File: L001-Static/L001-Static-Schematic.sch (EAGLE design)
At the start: 16 parts

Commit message: Fixes
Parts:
- R1, R2, R3, R4, R5, R6, R7, R8: value 10k -> 1K
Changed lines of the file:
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@@
 </classes>
 <parts>
-<part name="R1" library="resistor" deviceset="R-US_" device="VMTA55" value="10k"/>
-<part name="R2" library="resistor" deviceset="R-US_" device="VMTA55" value="10k"/>
-<part name="R3" library="resistor" deviceset="R-US_" device="VMTA55" value="10k"/>
-<part name="R4" library="resistor" deviceset="R-US_" device="VMTA55" value="10k"/>
-<part name="R5" library="resistor" deviceset="R-US_" device="VMTA55" value="10k"/>
-<part name="R6" library="resistor" deviceset="R-US_" device="VMTA55" value="10k"/>
-<part name="R7" library="resistor" deviceset="R-US_" device="VMTA55" value="10k"/>
-<part name="R8" library="resistor" deviceset="R-US_" device="VMTA55" value="10k"/>
+<part name="R1" library="resistor" deviceset="R-US_" device="VMTA55" value="1K"/>
+<part name="R2" library="resistor" deviceset="R-US_" device="VMTA55" value="1K"/>
+<part name="R3" library="resistor" deviceset="R-US_" device="VMTA55" value="1K"/>
+<part name="R4" library="resistor" deviceset="R-US_" device="VMTA55" value="1K"/>
+<part name="R5" library="resistor" deviceset="R-US_" device="VMTA55" value="1K"/>
+<part name="R6" library="resistor" deviceset="R-US_" device="VMTA55" value="1K"/>
+<part name="R7" library="resistor" deviceset="R-US_" device="VMTA55" value="1K"/>
+<part name="R8" library="resistor" deviceset="R-US_" device="VMTA55" value="1K"/>
 <part name="D1" library="diode" deviceset="1N581*" device="" technology="7-B" value="1N5817"/>
 <part name="D2" library="diode" deviceset="1N581*" device="" technology="7-B" value="1N5817"/>

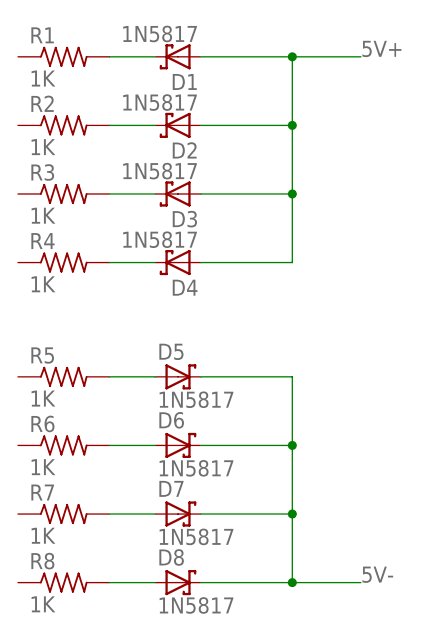
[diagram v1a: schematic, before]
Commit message: Update everything to use 1n60p Schottky diodes
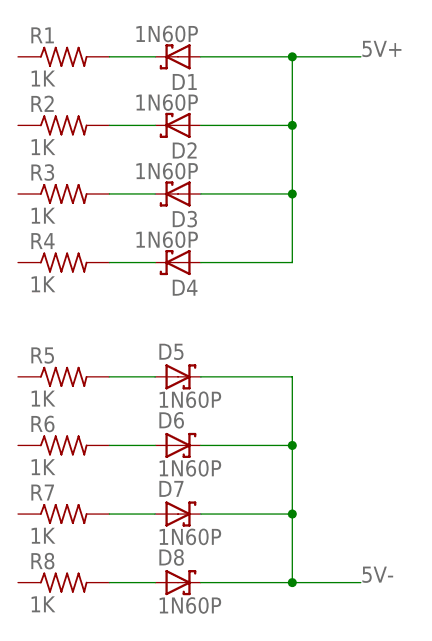
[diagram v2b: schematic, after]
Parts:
- D1, D2, D3, D4, D5, D6, D7, D8: value 1N5817 -> 1N60P
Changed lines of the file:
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@@
 <part name="R7" library="resistor" deviceset="R-US_" device="VMTA55" value="1K"/>
 <part name="R8" library="resistor" deviceset="R-US_" device="VMTA55" value="1K"/>
-<part name="D1" library="diode" deviceset="1N581*" device="" technology="7-B" value="1N5817"/>
-<part name="D2" library="diode" deviceset="1N581*" device="" technology="7-B" value="1N5817"/>
-<part name="D3" library="diode" deviceset="1N581*" device="" technology="7-B" value="1N5817"/>
-<part name="D4" library="diode" deviceset="1N581*" device="" technology="7-B" value="1N5817"/>
-<part name="D5" library="diode" deviceset="1N581*" device="" technology="7-B" value="1N5817"/>
-<part name="D6" library="diode" deviceset="1N581*" device="" technology="7-B" value="1N5817"/>
-<part name="D7" library="diode" deviceset="1N581*" device="" technology="7-B" value="1N5817"/>
-<part name="D8" library="diode" deviceset="1N581*" device="" technology="7-B" value="1N5817"/>
+<part name="D1" library="diode" deviceset="1N581*" device="" technology="7-B" value="1N60P"/>
+<part name="D2" library="diode" deviceset="1N581*" device="" technology="7-B" value="1N60P"/>
+<part name="D3" library="diode" deviceset="1N581*" device="" technology="7-B" value="1N60P"/>
+<part name="D4" library="diode" deviceset="1N581*" device="" technology="7-B" value="1N60P"/>
+<part name="D5" library="diode" deviceset="1N581*" device="" technology="7-B" value="1N60P"/>
+<part name="D6" library="diode" deviceset="1N581*" device="" technology="7-B" value="1N60P"/>
+<part name="D7" library="diode" deviceset="1N581*" device="" technology="7-B" value="1N60P"/>
+<part name="D8" library="diode" deviceset="1N581*" device="" technology="7-B" value="1N60P"/>
 </parts>
 <sheets>

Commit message: 10k r on outputs
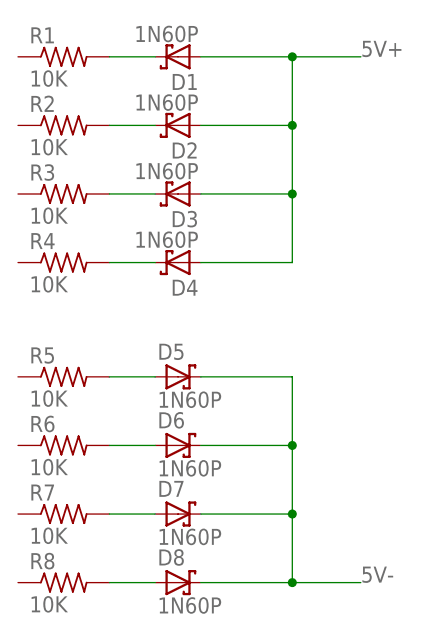
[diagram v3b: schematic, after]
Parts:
- R1, R2, R3, R4, R5, R6, R7, R8: value 1K -> 10K
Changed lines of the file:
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@@
 </classes>
 <parts>
-<part name="R1" library="resistor" deviceset="R-US_" device="VMTA55" value="1K"/>
-<part name="R2" library="resistor" deviceset="R-US_" device="VMTA55" value="1K"/>
-<part name="R3" library="resistor" deviceset="R-US_" device="VMTA55" value="1K"/>
-<part name="R4" library="resistor" deviceset="R-US_" device="VMTA55" value="1K"/>
-<part name="R5" library="resistor" deviceset="R-US_" device="VMTA55" value="1K"/>
-<part name="R6" library="resistor" deviceset="R-US_" device="VMTA55" value="1K"/>
-<part name="R7" library="resistor" deviceset="R-US_" device="VMTA55" value="1K"/>
-<part name="R8" library="resistor" deviceset="R-US_" device="VMTA55" value="1K"/>
+<part name="R1" library="resistor" deviceset="R-US_" device="VMTA55" value="10K"/>
+<part name="R2" library="resistor" deviceset="R-US_" device="VMTA55" value="10K"/>
+<part name="R3" library="resistor" deviceset="R-US_" device="VMTA55" value="10K"/>
+<part name="R4" library="resistor" deviceset="R-US_" device="VMTA55" value="10K"/>
+<part name="R5" library="resistor" deviceset="R-US_" device="VMTA55" value="10K"/>
+<part name="R6" library="resistor" deviceset="R-US_" device="VMTA55" value="10K"/>
+<part name="R7" library="resistor" deviceset="R-US_" device="VMTA55" value="10K"/>
+<part name="R8" library="resistor" deviceset="R-US_" device="VMTA55" value="10K"/>
 <part name="D1" library="diode" deviceset="1N581*" device="" technology="7-B" value="1N60P"/>
 <part name="D2" library="diode" deviceset="1N581*" device="" technology="7-B" value="1N60P"/>
